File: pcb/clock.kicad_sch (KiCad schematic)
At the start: 11 parts, among them J1 Conn_01x03_Pin, J2 Conn_01x03_Pin, J3 Conn_01x03_Pin, J4 Conn_01x03_Pin, U1 ESP32-C3-SuperMini

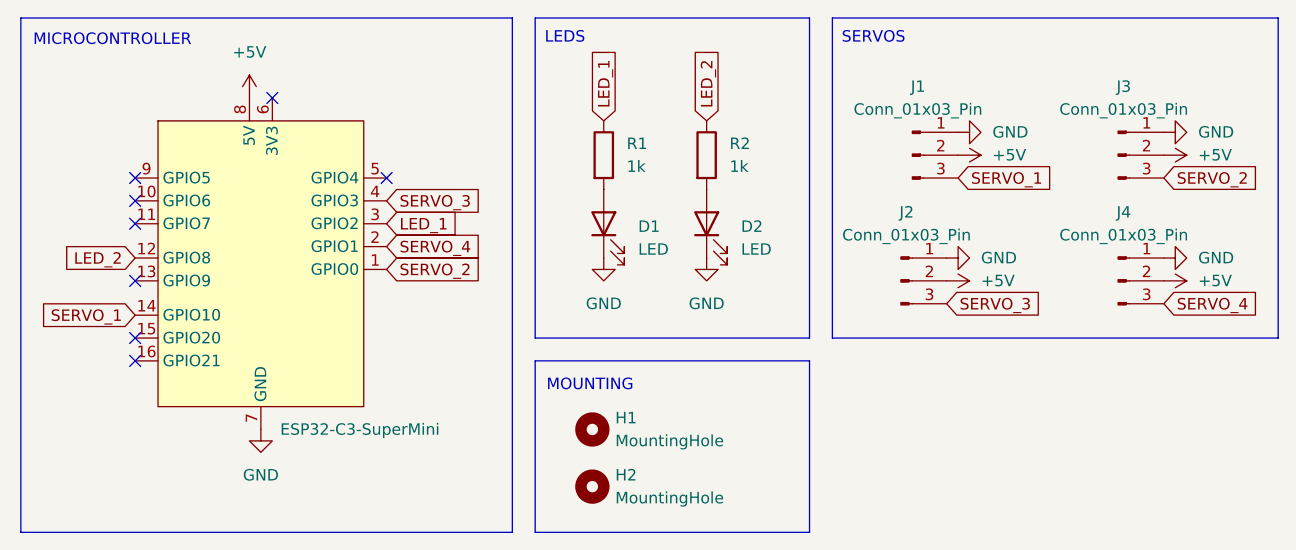
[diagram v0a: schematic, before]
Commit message: pcb: led improvements
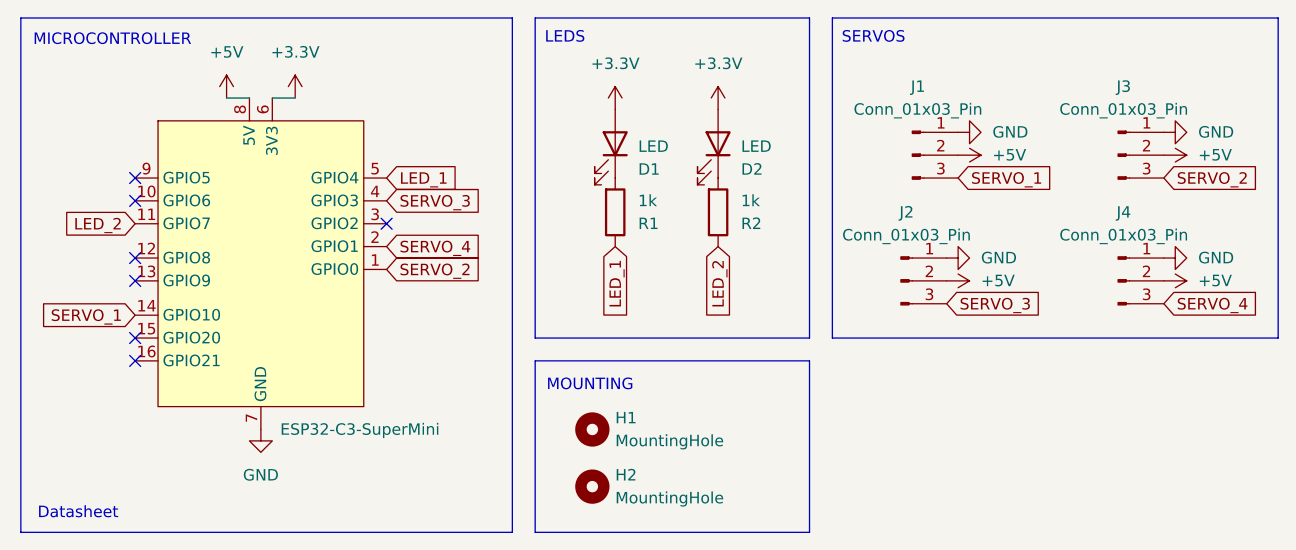
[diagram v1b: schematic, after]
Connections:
- net GND: no longer D1.1 (K), D2.1 (K)
- net LED_1: now also U1.5 (GPIO4); no longer U1.3 (GPIO2)
- net LED_2: now also U1.11 (GPIO7); no longer U1.12 (GPIO8)
- net +3.3V: now reaches U1.6 (3V3)
- net +3.3V: now also D1.2 (A), D2.2 (A)
- net at R1.2: now also D1.1 (K); no longer D1.2 (A)
- net at R2.2: now also D2.1 (K); no longer D2.2 (A)
- no-connect marks 8 -> 7
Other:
- note added: "Datasheet"
- moved on the sheet: D1, D2, R1, R2

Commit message: firmware: add esphome firmware
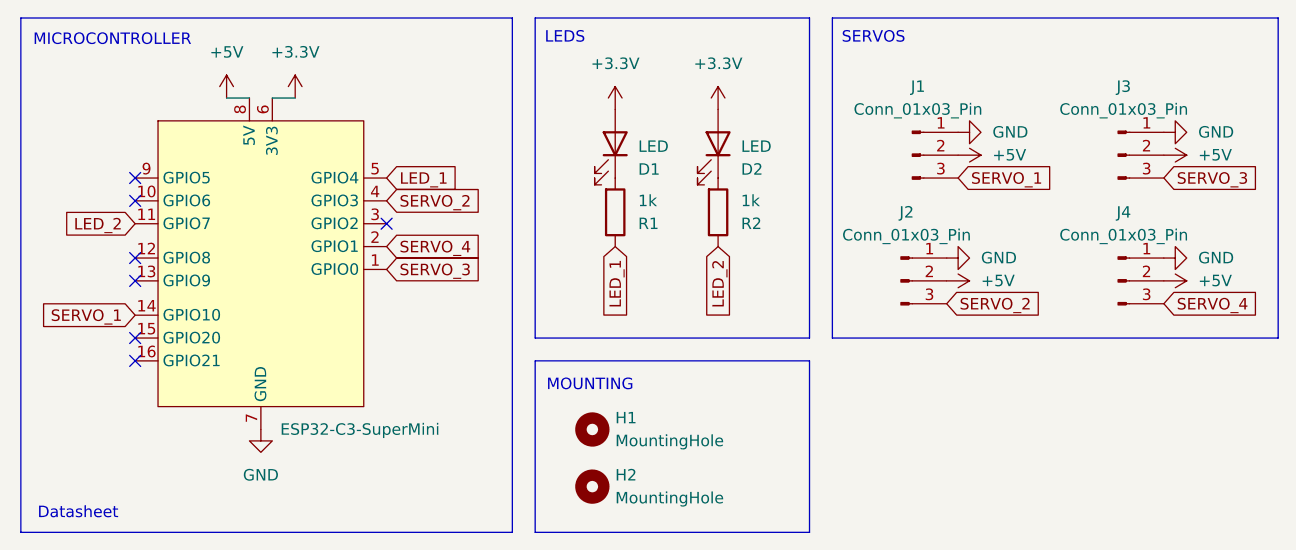
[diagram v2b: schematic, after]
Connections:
- net SERVO_2: now also J2.3 (Pin_3), U1.4 (GPIO3); no longer J3.3 (Pin_3), U1.1 (GPIO0)
- net SERVO_3: now also J3.3 (Pin_3), U1.1 (GPIO0); no longer J2.3 (Pin_3), U1.4 (GPIO3)
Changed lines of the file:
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@@
 	(global_label "SERVO_2"
 		(shape input)
+		(at 54.61 34.29 0)
+		(fields_autoplaced yes)
+		(effects
+			(font
+				(size 1.27 1.27)
+			)
+			(justify left)
+		)
+		(property "Intersheetrefs" "${INTERSHEET_REFS}"
+			(at 65.8199 34.29 0)
+			(hide yes)
+			(show_name no)
+			(do_not_autoplace no)
+			(effects
+				(font
+					(size 1.27 1.27)
+				)
+				(justify left)
+			)
+		)
+	)
+	(global_label "SERVO_4"
+		(shape input)
+		(at 54.61 39.37 0)
+		(fields_autoplaced yes)
+		(effects
+			(font
+				(size 1.27 1.27)
+			)
+			(justify left)
+		)
+		(property "Intersheetrefs" "${INTERSHEET_REFS}"
+			(at 65.8199 39.37 0)
+			(hide yes)
+			(show_name no)
+			(do_not_autoplace no)
+			(effects
+				(font
+					(size 1.27 1.27)
+				)
+				(justify left)
+			)
+		)
+	)
+	(global_label "SERVO_3"
+		(shape input)
+		(at 54.61 41.91 0)
+		(fields_autoplaced yes)
+		(effects
+			(font
+				(size 1.27 1.27)
+			)
+			(justify left)
+		)
+		(property "Intersheetrefs" "${INTERSHEET_REFS}"
+			(at 65.8199 41.91 0)
+			(hide yes)
+			(show_name no)
+			(do_not_autoplace no)
+			(effects
+				(font
+					(size 1.27 1.27)
+				)
+				(justify left)
+			)
+		)
+	)
+	(global_label "LED_2"
+		(shape input)
+		(at 91.44 39.37 270)
+		(fields_autoplaced yes)
+		(effects
+			(font
+				(size 1.27 1.27)
+			)
+			(justify right)
+		)
+		(property "Intersheetrefs" "${INTERSHEET_REFS}"
+			(at 91.44 47.9794 90)
+			(hide yes)
+			(show_name no)
+			(do_not_autoplace no)
+			(effects
+				(font
+					(size 1.27 1.27)
+				)
+				(justify right)
+			)
+		)
+	)
+	(global_label "LED_1"
+		(shape input)
+		(at 80.01 39.37 270)
+		(fields_autoplaced yes)
+		(effects
+			(font
+				(size 1.27 1.27)
+			)
+			(justify right)
+		)
+		(property "Intersheetrefs" "${INTERSHEET_REFS}"
+			(at 80.01 47.9794 90)
+			(hide yes)
+			(show_name no)
+			(do_not_autoplace no)
+			(effects
+				(font
+					(size 1.27 1.27)
+				)
+				(justify right)
+			)
+		)
+	)
+	(global_label "SERVO_1"
+		(shape input)
+		(at 26.67 46.99 180)
+		(fields_autoplaced yes)
+		(effects
+			(font
+				(size 1.27 1.27)
+			)
+			(justify right)
+		)
+		(property "Intersheetrefs" "${INTERSHEET_REFS}"
+			(at 15.4601 46.99 0)
+			(hide yes)
+			(show_name no)
+			(do_not_autoplace no)
+			(effects
+				(font
+					(size 1.27 1.27)
+				)
+				(justify right)
+			)
+		)
+	)
+	(global_label "SERVO_4"
+		(shape input)
+		(at 140.97 45.72 0)
+		(fields_autoplaced yes)
+		(effects
+			(font
+				(size 1.27 1.27)
+			)
+			(justify left)
+		)
+		(property "Intersheetrefs" "${INTERSHEET_REFS}"
+			(at 152.1799 45.72 0)
+			(hide yes)
+			(show_name no)
+			(do_not_autoplace no)
+			(effects
+				(font
+					(size 1.27 1.27)
+				)
+				(justify left)
+			)
+		)
+	)
+	(global_label "LED_1"
+		(shape input)
+		(at 54.61 31.75 0)
+		(fields_autoplaced yes)
+		(effects
+			(font
+				(size 1.27 1.27)
+			)
+			(justify left)
+		)
+		(property "Intersheetrefs" "${INTERSHEET_REFS}"
+			(at 63.2194 31.75 0)
+			(hide yes)
+			(show_name no)
+			(do_not_autoplace no)
+			(effects
+				(font
+					(size 1.27 1.27)
+				)
+				(justify left)
+			)
+		)
+	)
+	(global_label "LED_2"
+		(shape input)
+		(at 26.67 36.83 180)
+		(fields_autoplaced yes)
+		(effects
+			(font
+				(size 1.27 1.27)
+			)
+			(justify right)
+		)
+		(property "Intersheetrefs" "${INTERSHEET_REFS}"
+			(at 18.0606 36.83 0)
+			(hide yes)
+			(show_name no)
+			(do_not_autoplace no)
+			(effects
+				(font
+					(size 1.27 1.27)
+				)
+				(justify right)
+			)
+		)
+	)
+	(global_label "SERVO_3"
+		(shape input)
 		(at 140.97 31.75 0)
 		(fields_autoplaced yes)
@@
 		)
 	)
-	(global_label "SERVO_4"
-		(shape input)
-		(at 54.61 39.37 0)
-		(fields_autoplaced yes)
-		(effects
-			(font
-				(size 1.27 1.27)
-			)
-			(justify left)
-		)
-		(property "Intersheetrefs" "${INTERSHEET_REFS}"
-			(at 65.8199 39.37 0)
-			(hide yes)
-			(show_name no)
-			(do_not_autoplace no)
-			(effects
-				(font
-					(size 1.27 1.27)
-				)
-				(justify left)
-			)
-		)
-	)
-	(global_label "SERVO_3"
+	(global_label "SERVO_2"
 		(shape input)
 		(at 116.84 45.72 0)
@@
 			)
 		)
-	)
-	(global_label "LED_2"
-		(shape input)
-		(at 91.44 39.37 270)
-		(fields_autoplaced yes)
-		(effects
-			(font
-				(size 1.27 1.27)
-			)
-			(justify right)
-		)
-		(property "Intersheetrefs" "${INTERSHEET_REFS}"
-			(at 91.44 47.9794 90)
-			(hide yes)
-			(show_name no)
-			(do_not_autoplace no)
-			(effects
-				(font
-					(size 1.27 1.27)
-				)
-				(justify right)
-			)
-		)
-	)
-	(global_label "LED_1"
-		(shape input)
-		(at 80.01 39.37 270)
-		(fields_autoplaced yes)
-		(effects
-			(font
-				(size 1.27 1.27)
-			)
-			(justify right)
-		)
-		(property "Intersheetrefs" "${INTERSHEET_REFS}"
-			(at 80.01 47.9794 90)
-			(hide yes)
-			(show_name no)
-			(do_not_autoplace no)
-			(effects
-				(font
-					(size 1.27 1.27)
-				)
-				(justify right)
-			)
-		)
-	)
-	(global_label "SERVO_1"
-		(shape input)
-		(at 26.67 46.99 180)
-		(fields_autoplaced yes)
-		(effects
-			(font
-				(size 1.27 1.27)
-			)
-			(justify right)
-		)
-		(property "Intersheetrefs" "${INTERSHEET_REFS}"
-			(at 15.4601 46.99 0)
-			(hide yes)
-			(show_name no)
-			(do_not_autoplace no)
-			(effects
-				(font
-					(size 1.27 1.27)
-				)
-				(justify right)
-			)
-		)
-	)
-	(global_label "SERVO_3"
-		(shape input)
-		(at 54.61 34.29 0)
-		(fields_autoplaced yes)
-		(effects
-			(font
-				(size 1.27 1.27)
-			)
-			(justify left)
-		)
-		(property "Intersheetrefs" "${INTERSHEET_REFS}"
-			(at 65.8199 34.29 0)
-			(hide yes)
-			(show_name no)
-			(do_not_autoplace no)
-			(effects
-				(font
-					(size 1.27 1.27)
-				)
-				(justify left)
-			)
-		)
-	)
-	(global_label "SERVO_2"
-		(shape input)
-		(at 54.61 41.91 0)
-		(fields_autoplaced yes)
-		(effects
-			(font
-				(size 1.27 1.27)
-			)
-			(justify left)
-		)
-		(property "Intersheetrefs" "${INTERSHEET_REFS}"
-			(at 65.8199 41.91 0)
-			(hide yes)
-			(show_name no)
-			(do_not_autoplace no)
-			(effects
-				(font
-					(size 1.27 1.27)
-				)
-				(justify left)
-			)
-		)
-	)
-	(global_label "SERVO_4"
-		(shape input)
-		(at 140.97 45.72 0)
-		(fields_autoplaced yes)
-		(effects
-			(font
-				(size 1.27 1.27)
-			)
-			(justify left)
-		)
-		(property "Intersheetrefs" "${INTERSHEET_REFS}"
-			(at 152.1799 45.72 0)
-			(hide yes)
-			(show_name no)
-			(do_not_autoplace no)
-			(effects
-				(font
-					(size 1.27 1.27)
-				)
-				(justify left)
-			)
-		)
-	)
-	(global_label "LED_1"
-		(shape input)
-		(at 54.61 31.75 0)
-		(fields_autoplaced yes)
-		(effects
-			(font
-				(size 1.27 1.27)
-			)
-			(justify left)
-		)
-		(property "Intersheetrefs" "${INTERSHEET_REFS}"
-			(at 63.2194 31.75 0)
-			(hide yes)
-			(show_name no)
-			(do_not_autoplace no)
-			(effects
-				(font
-					(size 1.27 1.27)
-				)
-				(justify left)
-			)
-		)
-	)
-	(global_label "LED_2"
-		(shape input)
-		(at 26.67 36.83 180)
-		(fields_autoplaced yes)
-		(effects
-			(font
-				(size 1.27 1.27)
-			)
-			(justify right)
-		)
-		(property "Intersheetrefs" "${INTERSHEET_REFS}"
-			(at 18.0606 36.83 0)
-			(hide yes)
-			(show_name no)
-			(do_not_autoplace no)
-			(effects
-				(font
-					(size 1.27 1.27)
-				)
-				(justify right)
-			)
-		)
